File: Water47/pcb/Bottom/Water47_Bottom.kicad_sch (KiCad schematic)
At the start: 7 parts, among them U1 MOUDLE-SEEEDUINO-XIAO

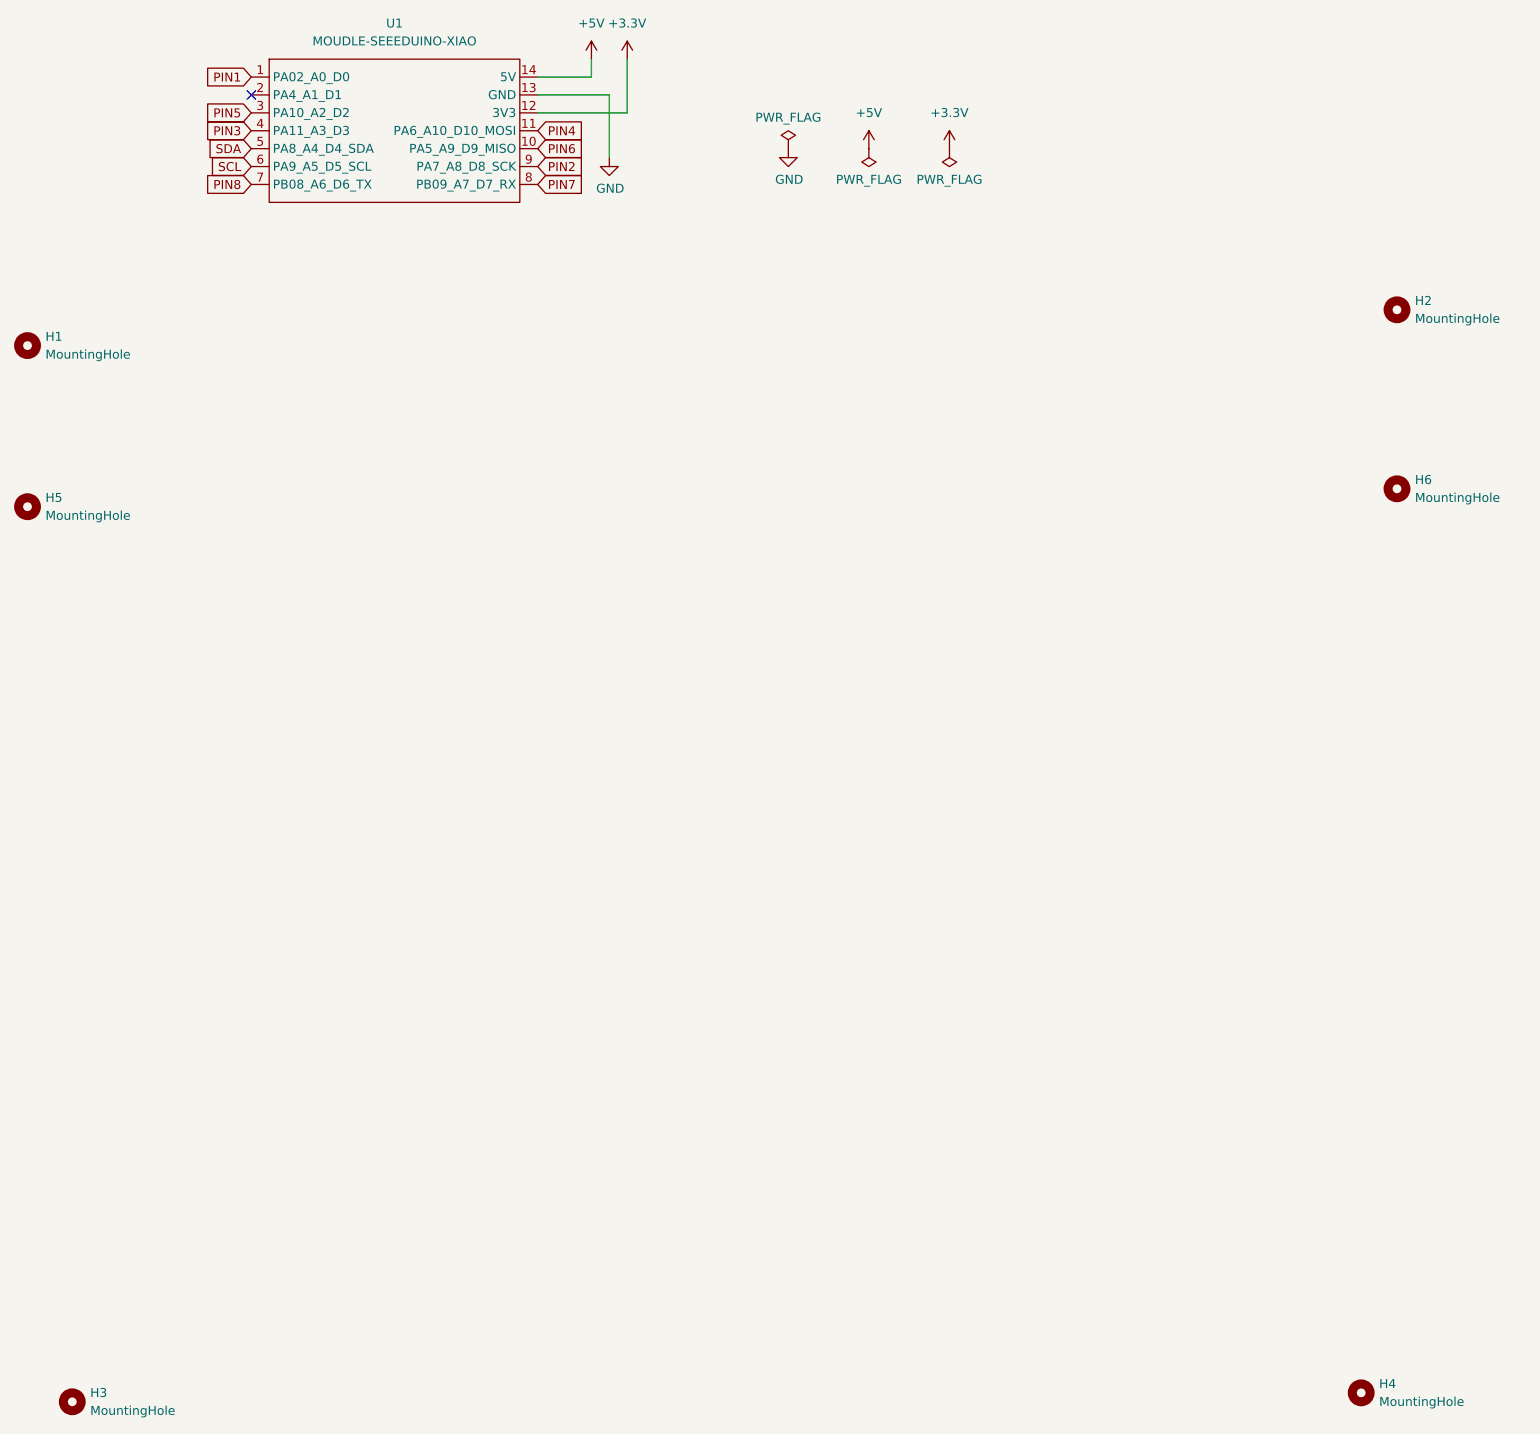
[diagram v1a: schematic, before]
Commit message: feat: add mounting hole, set gerber path
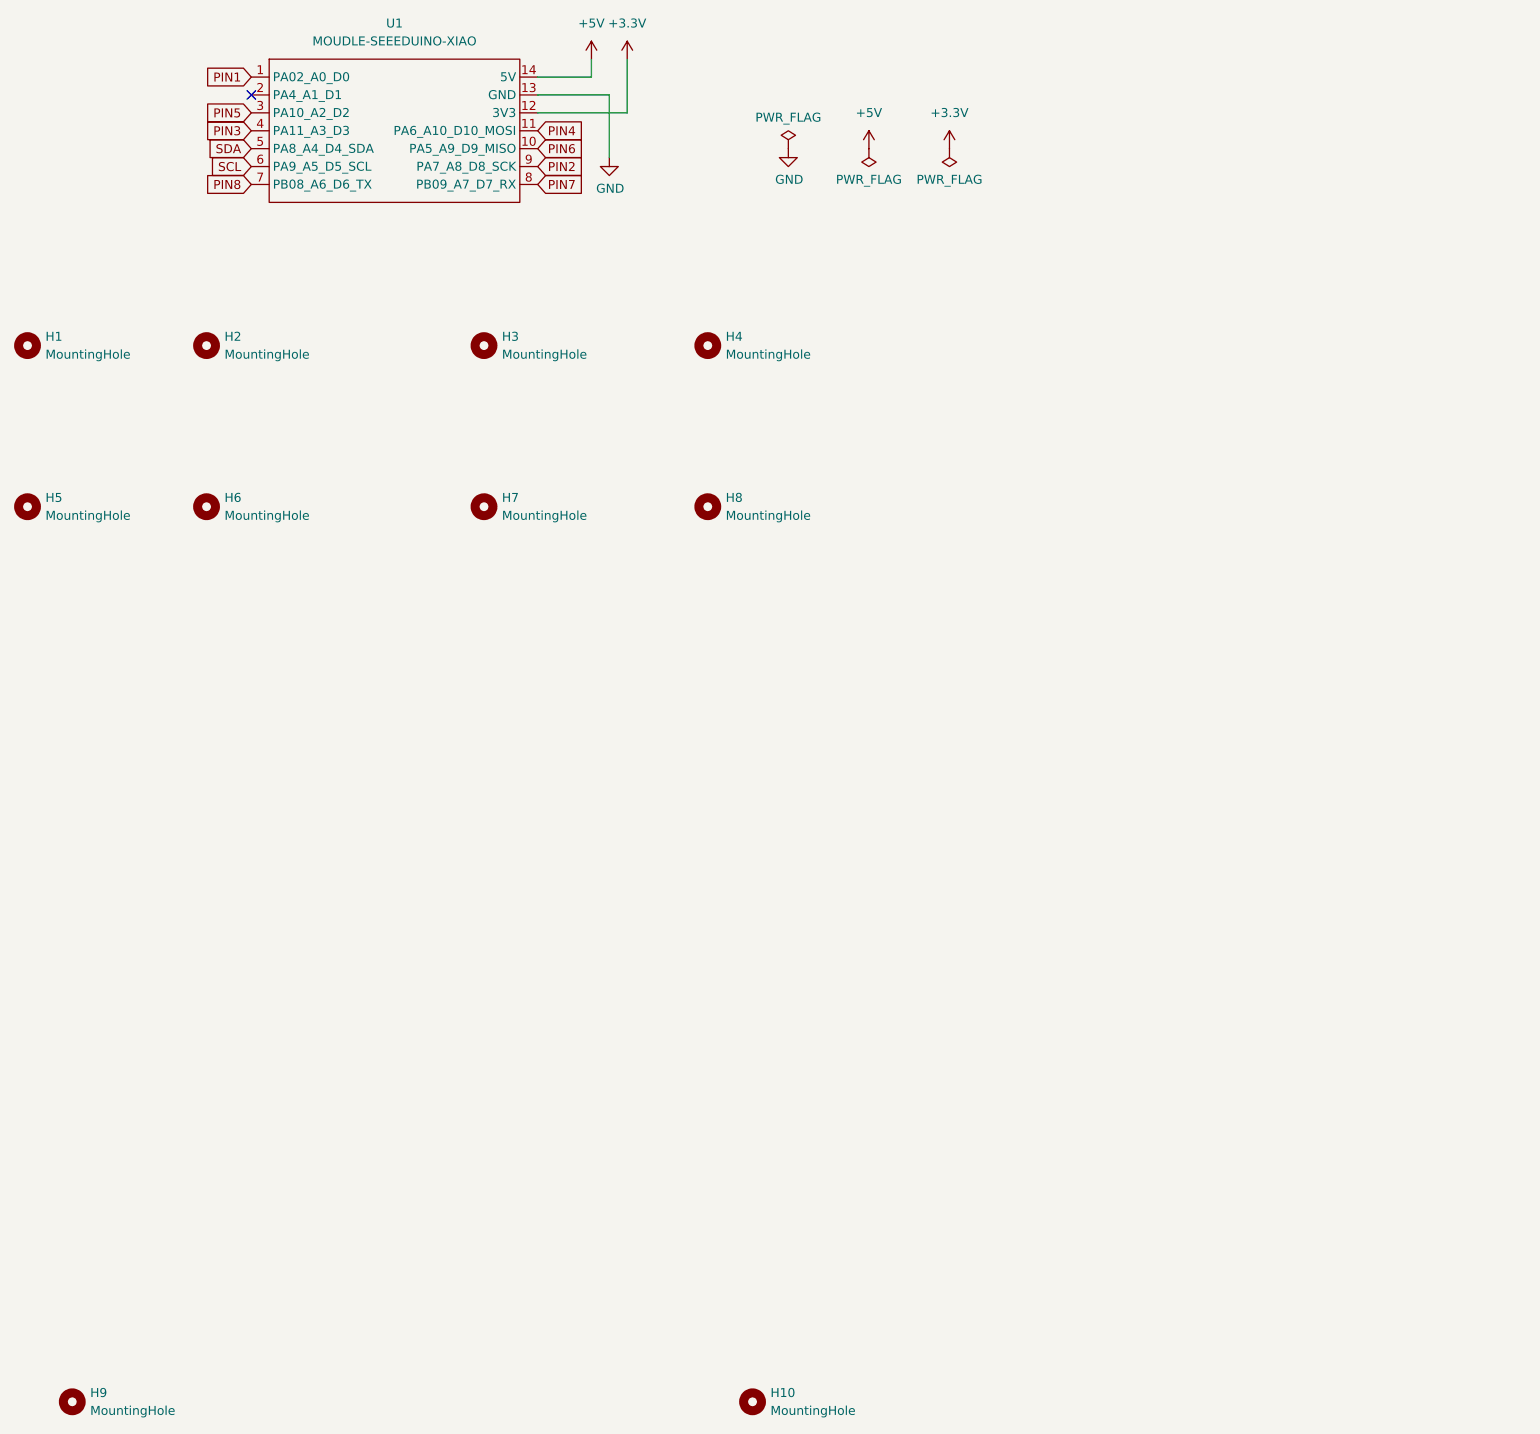
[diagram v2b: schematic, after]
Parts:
- added H2, H3, H6, H7: MountingHole, kbd_Hole:m2_Screw_Hole, symbol Mechanical:MountingHole
- renumbered H4 to H10, H2 to H4, H6 to H8, H3 to H9
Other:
- moved on the sheet: H10, H4, H8
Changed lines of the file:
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@@
     (pin "1")
+  )
+  (symbol (lib_id "Mechanical:MountingHole") (at 48.26 91.44 0) (unit 1)
+    (in_bom yes) (on_board yes) (fields_autoplaced)
+    (property "Reference" "H6" (id 0) (at 50.8 90.1699 0)
+      (effects (font (size 1.27 1.27)) (justify left))
+    )
+    (property "Value" "MountingHole" (id 1) (at 50.8 92.7099 0)
+      (effects (font (size 1.27 1.27)) (justify left))
+    )
+    (property "Footprint" "kbd_Hole:m2_Screw_Hole" (id 2) (at 48.26 91.44 0)
+      (effects (font (size 1.27 1.27)) hide)
+    )
+    (property "Datasheet" "~" (id 3) (at 48.26 91.44 0)
+      (effects (font (size 1.27 1.27)) hide)
+    )
   )
   (symbol (lib_id "power:PWR_FLAG") (at 142.24 40.64 180) (unit 1)
@@
     (pin "1")
   )
-  (symbol (lib_id "Mechanical:MountingHole") (at 217.17 88.9 0) (unit 1)
-    (in_bom yes) (on_board yes) (fields_autoplaced)
-    (property "Reference" "H6" (id 0) (at 219.71 87.6299 0)
-      (effects (font (size 1.27 1.27)) (justify left))
-    )
-    (property "Value" "MountingHole" (id 1) (at 219.71 90.1699 0)
-      (effects (font (size 1.27 1.27)) (justify left))
-    )
-    (property "Footprint" "kbd_Hole:m2_Screw_Hole" (id 2) (at 217.17 88.9 0)
-      (effects (font (size 1.27 1.27)) hide)
-    )
-    (property "Datasheet" "~" (id 3) (at 217.17 88.9 0)
+  (symbol (lib_id "Mechanical:MountingHole") (at 119.38 91.44 0) (unit 1)
+    (in_bom yes) (on_board yes) (fields_autoplaced)
+    (property "Reference" "H8" (id 0) (at 121.92 90.1699 0)
+      (effects (font (size 1.27 1.27)) (justify left))
+    )
+    (property "Value" "MountingHole" (id 1) (at 121.92 92.7099 0)
+      (effects (font (size 1.27 1.27)) (justify left))
+    )
+    (property "Footprint" "kbd_Hole:m2_Screw_Hole" (id 2) (at 119.38 91.44 0)
+      (effects (font (size 1.27 1.27)) hide)
+    )
+    (property "Datasheet" "~" (id 3) (at 119.38 91.44 0)
       (effects (font (size 1.27 1.27)) hide)
     )
@@
     (pin "1")
   )
+  (symbol (lib_id "Mechanical:MountingHole") (at 87.63 68.58 0) (unit 1)
+    (in_bom yes) (on_board yes) (fields_autoplaced)
+    (property "Reference" "H3" (id 0) (at 90.17 67.3099 0)
+      (effects (font (size 1.27 1.27)) (justify left))
+    )
+    (property "Value" "MountingHole" (id 1) (at 90.17 69.8499 0)
+      (effects (font (size 1.27 1.27)) (justify left))
+    )
+    (property "Footprint" "kbd_Hole:m2_Screw_Hole" (id 2) (at 87.63 68.58 0)
+      (effects (font (size 1.27 1.27)) hide)
+    )
+    (property "Datasheet" "~" (id 3) (at 87.63 68.58 0)
+      (effects (font (size 1.27 1.27)) hide)
+    )
+  )
+  (symbol (lib_id "Mechanical:MountingHole") (at 48.26 68.58 0) (unit 1)
+    (in_bom yes) (on_board yes) (fields_autoplaced)
+    (property "Reference" "H2" (id 0) (at 50.8 67.3099 0)
+      (effects (font (size 1.27 1.27)) (justify left))
+    )
+    (property "Value" "MountingHole" (id 1) (at 50.8 69.8499 0)
+      (effects (font (size 1.27 1.27)) (justify left))
+    )
+    (property "Footprint" "kbd_Hole:m2_Screw_Hole" (id 2) (at 48.26 68.58 0)
+      (effects (font (size 1.27 1.27)) hide)
+    )
+    (property "Datasheet" "~" (id 3) (at 48.26 68.58 0)
+      (effects (font (size 1.27 1.27)) hide)
+    )
+  )
   (symbol (lib_id "power:+3.3V") (at 107.95 27.94 0) (unit 1)
     (in_bom yes) (on_board yes) (fields_autoplaced)
@@
   (symbol (lib_id "Mechanical:MountingHole") (at 29.21 218.44 0) (unit 1)
     (in_bom yes) (on_board yes) (fields_autoplaced)
-    (property "Reference" "H3" (id 0) (at 31.75 217.1699 0)
+    (property "Reference" "H9" (id 0) (at 31.75 217.1699 0)
       (effects (font (size 1.27 1.27)) (justify left))
     )
@@
     )
   )
-  (symbol (lib_id "Mechanical:MountingHole") (at 212.09 217.17 0) (unit 1)
-    (in_bom yes) (on_board yes) (fields_autoplaced)
-    (property "Reference" "H4" (id 0) (at 214.63 215.8999 0)
-      (effects (font (size 1.27 1.27)) (justify left))
-    )
-    (property "Value" "MountingHole" (id 1) (at 214.63 218.4399 0)
-      (effects (font (size 1.27 1.27)) (justify left))
-    )
-    (property "Footprint" "kbd_Hole:m2_Screw_Hole" (id 2) (at 212.09 217.17 0)
-      (effects (font (size 1.27 1.27)) hide)
-    )
-    (property "Datasheet" "~" (id 3) (at 212.09 217.17 0)
+  (symbol (lib_id "Mechanical:MountingHole") (at 125.73 218.44 0) (unit 1)
+    (in_bom yes) (on_board yes) (fields_autoplaced)
+    (property "Reference" "H10" (id 0) (at 128.27 217.1699 0)
+      (effects (font (size 1.27 1.27)) (justify left))
+    )
+    (property "Value" "MountingHole" (id 1) (at 128.27 219.7099 0)
+      (effects (font (size 1.27 1.27)) (justify left))
+    )
+    (property "Footprint" "kbd_Hole:m2_Screw_Hole" (id 2) (at 125.73 218.44 0)
+      (effects (font (size 1.27 1.27)) hide)
+    )
+    (property "Datasheet" "~" (id 3) (at 125.73 218.44 0)
       (effects (font (size 1.27 1.27)) hide)
     )
@@
     (pin "9")
   )
+  (symbol (lib_id "Mechanical:MountingHole") (at 87.63 91.44 0) (unit 1)
+    (in_bom yes) (on_board yes) (fields_autoplaced)
+    (property "Reference" "H7" (id 0) (at 90.17 90.1699 0)
+      (effects (font (size 1.27 1.27)) (justify left))
+    )
+    (property "Value" "MountingHole" (id 1) (at 90.17 92.7099 0)
+      (effects (font (size 1.27 1.27)) (justify left))
+    )
+    (property "Footprint" "kbd_Hole:m2_Screw_Hole" (id 2) (at 87.63 91.44 0)
+      (effects (font (size 1.27 1.27)) hide)
+    )
+    (property "Datasheet" "~" (id 3) (at 87.63 91.44 0)
+      (effects (font (size 1.27 1.27)) hide)
+    )
+  )
   (symbol (lib_id "power:GND") (at 105.41 41.91 0) (unit 1)
     (in_bom yes) (on_board yes)
@@
     (pin "1")
   )
-  (symbol (lib_id "Mechanical:MountingHole") (at 217.17 63.5 0) (unit 1)
-    (in_bom yes) (on_board yes) (fields_autoplaced)
-    (property "Reference" "H2" (id 0) (at 219.71 62.2299 0)
-      (effects (font (size 1.27 1.27)) (justify left))
-    )
-    (property "Value" "MountingHole" (id 1) (at 219.71 64.7699 0)
-      (effects (font (size 1.27 1.27)) (justify left))
-    )
-    (property "Footprint" "kbd_Hole:m2_Screw_Hole" (id 2) (at 217.17 63.5 0)
-      (effects (font (size 1.27 1.27)) hide)
-    )
-    (property "Datasheet" "~" (id 3) (at 217.17 63.5 0)
+  (symbol (lib_id "Mechanical:MountingHole") (at 119.38 68.58 0) (unit 1)
+    (in_bom yes) (on_board yes) (fields_autoplaced)
+    (property "Reference" "H4" (id 0) (at 121.92 67.3099 0)
+      (effects (font (size 1.27 1.27)) (justify left))
+    )
+    (property "Value" "MountingHole" (id 1) (at 121.92 69.8499 0)
+      (effects (font (size 1.27 1.27)) (justify left))
+    )
+    (property "Footprint" "kbd_Hole:m2_Screw_Hole" (id 2) (at 119.38 68.58 0)
+      (effects (font (size 1.27 1.27)) hide)
+    )
+    (property "Datasheet" "~" (id 3) (at 119.38 68.58 0)
       (effects (font (size 1.27 1.27)) hide)
     )
@@
       (reference "H1") (unit 1) (value "MountingHole") (footprint "kbd_Hole:m2_Screw_Hole")
     )
+    (path "/7290d1da-ca5e-44b0-b48d-1703ad5e3244"
+      (reference "H2") (unit 1) (value "MountingHole") (footprint "kbd_Hole:m2_Screw_Hole")
+    )
+    (path "/70c278fa-bc20-4154-a626-b7849bd0c859"
+      (reference "H3") (unit 1) (value "MountingHole") (footprint "kbd_Hole:m2_Screw_Hole")
+    )
     (path "/f64ccafc-8d73-4e0d-a0a9-52c38f87dc6c"
-      (reference "H2") (unit 1) (value "MountingHole") (footprint "kbd_Hole:m2_Screw_Hole")
-    )
-    (path "/bbde9b31-2ca1-42cc-a23f-bd08fc375c76"
-      (reference "H3") (unit 1) (value "MountingHole") (footprint "kbd_Hole:m2_Screw_Hole")
-    )
-    (path "/caa5335b-ab47-478f-b510-96296c076797"
       (reference "H4") (unit 1) (value "MountingHole") (footprint "kbd_Hole:m2_Screw_Hole")
     )
@@
       (reference "H5") (unit 1) (value "MountingHole") (footprint "kbd_Hole:m2_Screw_Hole")
     )
+    (path "/4f92cc55-0938-4e95-9de8-b2772bc65699"
+      (reference "H6") (unit 1) (value "MountingHole") (footprint "kbd_Hole:m2_Screw_Hole")
+    )
+    (path "/e4fff868-125d-421d-95a7-f22604281eea"
+      (reference "H7") (unit 1) (value "MountingHole") (footprint "kbd_Hole:m2_Screw_Hole")
+    )
     (path "/5baf0ae5-116d-4142-b157-7cb2ebe3f02d"
-      (reference "H6") (unit 1) (value "MountingHole") (footprint "kbd_Hole:m2_Screw_Hole")
+      (reference "H8") (unit 1) (value "MountingHole") (footprint "kbd_Hole:m2_Screw_Hole")
+    )
+    (path "/bbde9b31-2ca1-42cc-a23f-bd08fc375c76"
+      (reference "H9") (unit 1) (value "MountingHole") (footprint "kbd_Hole:m2_Screw_Hole")
+    )
+    (path "/caa5335b-ab47-478f-b510-96296c076797"
+      (reference "H10") (unit 1) (value "MountingHole") (footprint "kbd_Hole:m2_Screw_Hole")
     )
     (path "/d703529e-35b6-4856-b4e1-4ebcffe81b73"
